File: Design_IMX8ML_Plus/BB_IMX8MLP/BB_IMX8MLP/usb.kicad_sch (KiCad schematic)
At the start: 31 parts, among them U3 USB5744_2G, Y1 25MHz

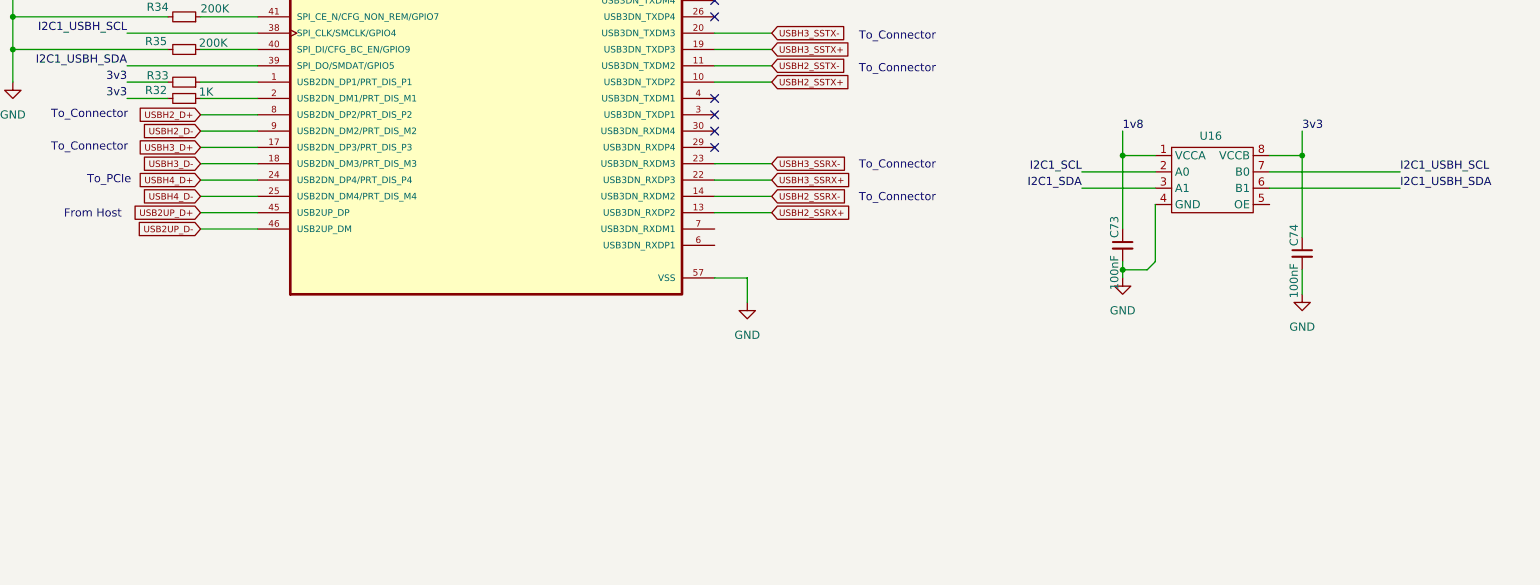
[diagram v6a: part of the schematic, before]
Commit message: reorganization of the componentes
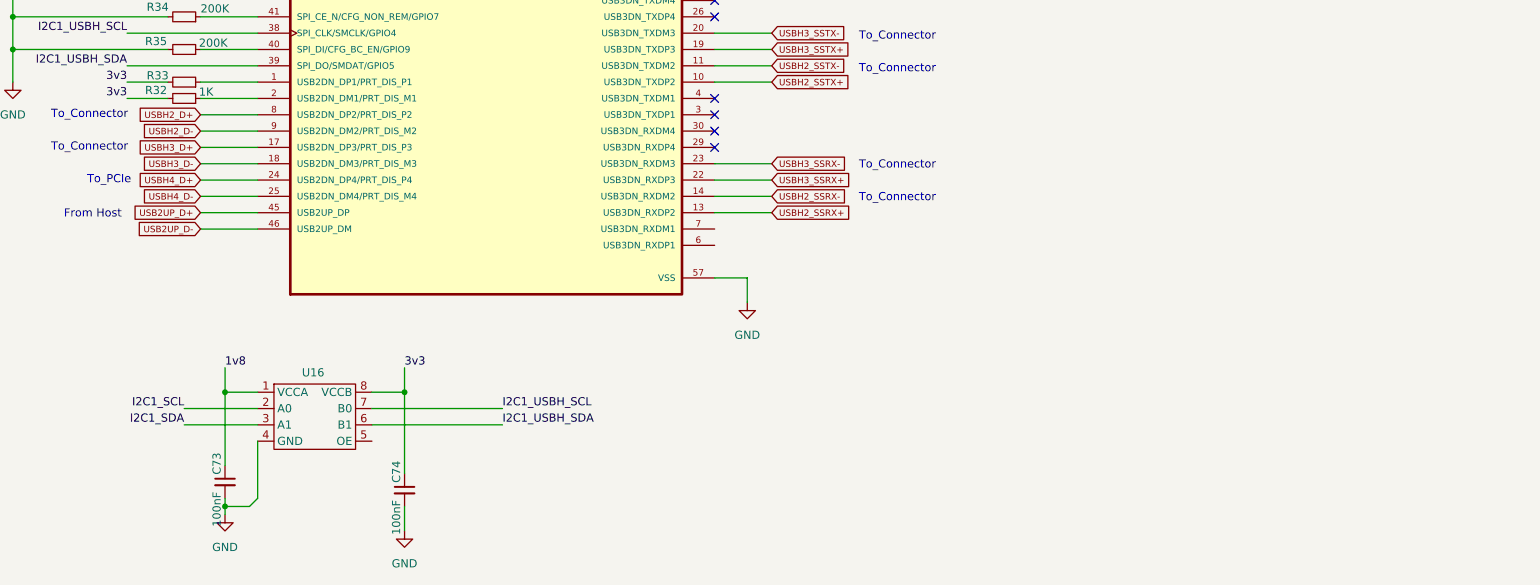
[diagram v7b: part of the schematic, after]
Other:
- moved on the sheet: C73, C74, U16
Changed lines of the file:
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@@
 	)
 	(junction
-		(at 204.47 123.19)
+		(at 64.77 160.02)
 		(diameter 0)
 		(color 0 0 0 0)
@@
 	)
 	(junction
-		(at 232.41 123.19)
+		(at 92.71 160.02)
 		(diameter 0)
 		(color 0 0 0 0)
@@
 	)
 	(junction
-		(at 204.47 140.97)
+		(at 64.77 177.8)
 		(diameter 0)
 		(color 0 0 0 0)
@@
 	(wire
 		(pts
-			(xy 247.65 128.27) (xy 227.33 128.27)
+			(xy 107.95 165.1) (xy 87.63 165.1)
 		)
 		(stroke
@@
 	(wire
 		(pts
-			(xy 204.47 140.97) (xy 204.47 142.24)
+			(xy 64.77 177.8) (xy 64.77 179.07)
 		)
 		(stroke
@@
 	(wire
 		(pts
-			(xy 227.33 123.19) (xy 232.41 123.19)
+			(xy 87.63 160.02) (xy 92.71 160.02)
 		)
 		(stroke
@@
 	(wire
 		(pts
-			(xy 232.41 140.97) (xy 232.41 144.78)
+			(xy 92.71 177.8) (xy 92.71 181.61)
 		)
 		(stroke
@@
 	(wire
 		(pts
-			(xy 204.47 119.38) (xy 204.47 123.19)
+			(xy 64.77 156.21) (xy 64.77 160.02)
 		)
 		(stroke
@@
 	(wire
 		(pts
-			(xy 204.47 123.19) (xy 204.47 134.62)
+			(xy 64.77 160.02) (xy 64.77 171.45)
 		)
 		(stroke
@@
 	(wire
 		(pts
-			(xy 204.47 140.97) (xy 208.28 140.97)
+			(xy 64.77 177.8) (xy 68.58 177.8)
 		)
 		(stroke
@@
 	(wire
 		(pts
-			(xy 198.12 128.27) (xy 209.55 128.27)
+			(xy 58.42 165.1) (xy 69.85 165.1)
 		)
 		(stroke
@@
 	(wire
 		(pts
-			(xy 232.41 123.19) (xy 232.41 135.89)
+			(xy 92.71 160.02) (xy 92.71 172.72)
 		)
 		(stroke
@@
 	(wire
 		(pts
-			(xy 209.55 130.81) (xy 209.55 139.7)
+			(xy 69.85 167.64) (xy 69.85 176.53)
 		)
 		(stroke
@@
 	(wire
 		(pts
-			(xy 198.12 125.73) (xy 209.55 125.73)
+			(xy 58.42 162.56) (xy 69.85 162.56)
 		)
 		(stroke
@@
 	(wire
 		(pts
-			(xy 247.65 125.73) (xy 227.33 125.73)
+			(xy 107.95 162.56) (xy 87.63 162.56)
 		)
 		(stroke
@@
 	(wire
 		(pts
-			(xy 204.47 139.7) (xy 204.47 140.97)
+			(xy 64.77 176.53) (xy 64.77 177.8)
 		)
 		(stroke
@@
 	(wire
 		(pts
-			(xy 208.28 140.97) (xy 209.55 139.7)
+			(xy 68.58 177.8) (xy 69.85 176.53)
 		)
 		(stroke
@@
 	(wire
 		(pts
-			(xy 209.55 123.19) (xy 204.47 123.19)
+			(xy 69.85 160.02) (xy 64.77 160.02)
 		)
 		(stroke
@@
 	(wire
 		(pts
-			(xy 232.41 119.38) (xy 232.41 123.19)
+			(xy 92.71 156.21) (xy 92.71 160.02)
 		)
 		(stroke
@@
 	)
 	(label "1v8"
-		(at 204.47 119.38 0)
+		(at 64.77 156.21 0)
 		(effects
 			(font
@@
 	)
 	(label "I2C1_SCL"
-		(at 198.12 125.73 180)
+		(at 58.42 162.56 180)
 		(effects
 			(font
@@
 	)
 	(label "I2C1_USBH_SCL"
-		(at 247.65 125.73 0)
+		(at 107.95 162.56 0)
 		(effects
 			(font
@@
 	)
 	(label "I2C1_SDA"
-		(at 198.12 128.27 180)
+		(at 58.42 165.1 180)
 		(effects
 			(font
@@
 	)
 	(label "I2C1_USBH_SDA"
-		(at 247.65 128.27 0)
+		(at 107.95 165.1 0)
 		(effects
 			(font
@@
 	)
 	(label "3v3"
-		(at 232.41 119.38 0)
+		(at 92.71 156.21 0)
 		(effects
 			(font
@@
 	(symbol
 		(lib_id "Device:C_Small")
-		(at 232.41 138.43 0)
+		(at 92.71 175.26 0)
 		(unit 1)
 		(exclude_from_sim no)
@@
 		(dnp no)
 		(property "Reference" "C74"
-			(at 231.14 133.858 90)
+			(at 91.44 170.688 90)
 			(effects
 				(font
@@
 		)
 		(property "Value" "100nF"
-			(at 231.14 139.954 90)
+			(at 91.44 176.784 90)
 			(effects
 				(font
@@
 		)
 		(property "Footprint" "Capacitor_SMD:C_0402_1005Metric"
-			(at 232.41 138.43 0)
+			(at 92.71 175.26 0)
 			(effects
 				(font
@@
 		)
 		(property "Datasheet" "~"
-			(at 232.41 138.43 0)
+			(at 92.71 175.26 0)
 			(effects
 				(font
@@
 		)
 		(property "Description" "Unpolarized capacitor, small symbol"
-			(at 232.41 138.43 0)
+			(at 92.71 175.26 0)
 			(effects
 				(font
@@
 	(symbol
 		(lib_id "power:GND")
-		(at 232.41 144.78 0)
+		(at 92.71 181.61 0)
 		(unit 1)
 		(exclude_from_sim no)
@@
 		(fields_autoplaced yes)
 		(property "Reference" "#PWR115"
-			(at 232.41 151.13 0)
+			(at 92.71 187.96 0)
 			(effects
 				(font
@@
 		)
 		(property "Value" "GND"
-			(at 232.41 149.86 0)
+			(at 92.71 186.69 0)
 			(effects
 				(font
@@
 		)
 		(property "Footprint" ""
-			(at 232.41 144.78 0)
+			(at 92.71 181.61 0)
 			(effects
 				(font
@@
 		)
 		(property "Datasheet" ""
-			(at 232.41 144.78 0)
+			(at 92.71 181.61 0)
 			(effects
 				(font
@@
 		)
 		(property "Description" "Power symbol creates a global label with name \"GND\" , ground"
-			(at 232.41 144.78 0)
+			(at 92.71 181.61 0)
 			(effects
 				(font
@@
 	(symbol
 		(lib_id "power:GND")
-		(at 204.47 142.24 0)
+		(at 64.77 179.07 0)
 		(unit 1)
 		(exclude_from_sim no)
@@
 		(fields_autoplaced yes)
 		(property "Reference" "#PWR114"
-			(at 204.47 148.59 0)
+			(at 64.77 185.42 0)
 			(effects
 				(font
@@
 		)
 		(property "Value" "GND"
-			(at 204.47 147.32 0)
+			(at 64.77 184.15 0)
 			(effects
 				(font
@@
 		)
 		(property "Footprint" ""
-			(at 204.47 142.24 0)
+			(at 64.77 179.07 0)
 			(effects
 				(font
@@
 		)
 		(property "Datasheet" ""
-			(at 204.47 142.24 0)
+			(at 64.77 179.07 0)
 			(effects
 				(font
@@
 		)
 		(property "Description" "Power symbol creates a global label with name \"GND\" , ground"
-			(at 204.47 142.24 0)
+			(at 64.77 179.07 0)
 			(effects
 				(font
@@
 	(symbol
 		(lib_id "_W_MX8M:FXMA2102L8X")
-		(at 217.17 129.54 0)
+		(at 77.47 166.37 0)
 		(unit 1)
 		(exclude_from_sim no)
@@
 		(dnp no)
 		(property "Reference" "U16"
-			(at 218.186 120.142 0)
+			(at 78.486 156.972 0)
 			(effects
 				(font
@@
 		)
 		(property "Value" "~"
-			(at 218.44 120.65 0)
+			(at 78.74 157.48 0)
 			(effects
 				(font
@@
 		)
 		(property "Footprint" "_W_SBC:MICROPAK8_1P6X1P6_ONS"
-			(at 217.17 129.54 0)
+			(at 77.47 166.37 0)
 			(effects
 				(font
@@
 		)
 		(property "Datasheet" ""
-			(at 217.17 129.54 0)
+			(at 77.47 166.37 0)
 			(effects
 				(font
@@
 		)
 		(property "Description" ""
-			(at 217.17 129.54 0)
+			(at 77.47 166.37 0)
 			(effects
 				(font
@@
 	(symbol
 		(lib_id "Device:C_Small")
-		(at 204.47 137.16 0)
+		(at 64.77 173.99 0)
 		(unit 1)
 		(exclude_from_sim no)
@@
 		(dnp no)
 		(property "Reference" "C73"
-			(at 203.2 132.588 90)
+			(at 63.5 169.418 90)
 			(effects
 				(font
@@
 		)
 		(property "Value" "100nF"
-			(at 203.2 138.684 90)
+			(at 63.5 175.514 90)
 			(effects
 				(font
@@
 		)
 		(property "Footprint" "Capacitor_SMD:C_0402_1005Metric"
-			(at 204.47 137.16 0)
+			(at 64.77 173.99 0)
 			(effects
 				(font
@@
 		)
 		(property "Datasheet" "~"
-			(at 204.47 137.16 0)
+			(at 64.77 173.99 0)
 			(effects
 				(font
@@
 		)
 		(property "Description" "Unpolarized capacitor, small symbol"
-			(at 204.47 137.16 0)
+			(at 64.77 173.99 0)
 			(effects
 				(font

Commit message: CPU Board actualizate
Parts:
- U3: footprint _W_SBC:QFN40P700X700X100-57N -> USB5744_2G:QFN40P700X700X100-57N
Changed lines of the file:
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@@
 			)
 		)
-		(property "Footprint" "_W_SBC:QFN40P700X700X100-57N"
+		(property "Footprint" "USB5744_2G:QFN40P700X700X100-57N"
 			(at 105.41 106.68 0)
 			(effects
